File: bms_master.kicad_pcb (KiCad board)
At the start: 4 copper layers, 78 x 59 mm, 73 parts, among them J1 Conn_01x08, J2 I2C, J3 I2C, J4 CSENSE, J5 CSENSE, J6 SWD, SW1 SW_Push, U1 TPS7B88, U2 MCP1700x-330xxMB, U3 STM32F103C8Tx, U4 SN65HVD1050D, U5 M24C64-R, U6 MAX6126, U7 MAX11163, U8 741G3157, Y1 8M

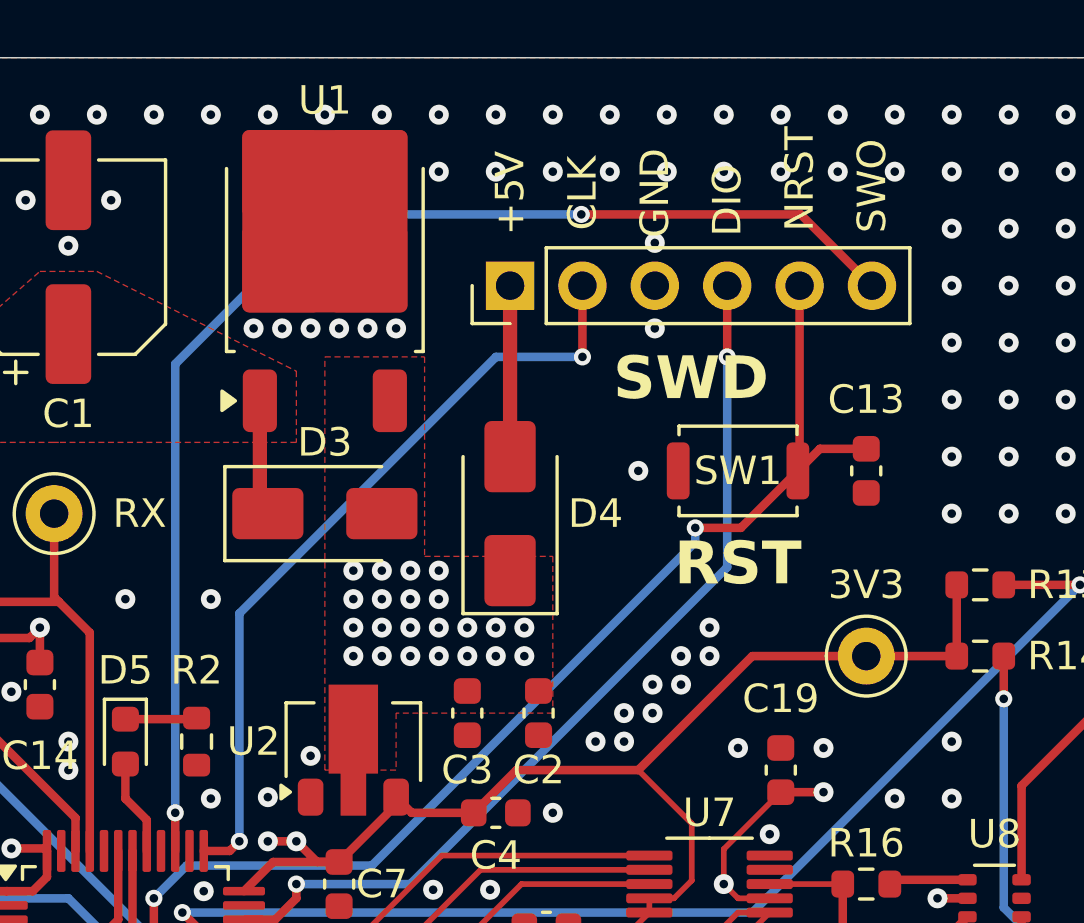
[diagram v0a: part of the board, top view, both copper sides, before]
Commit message: *: Update library references and move SWD header slightly
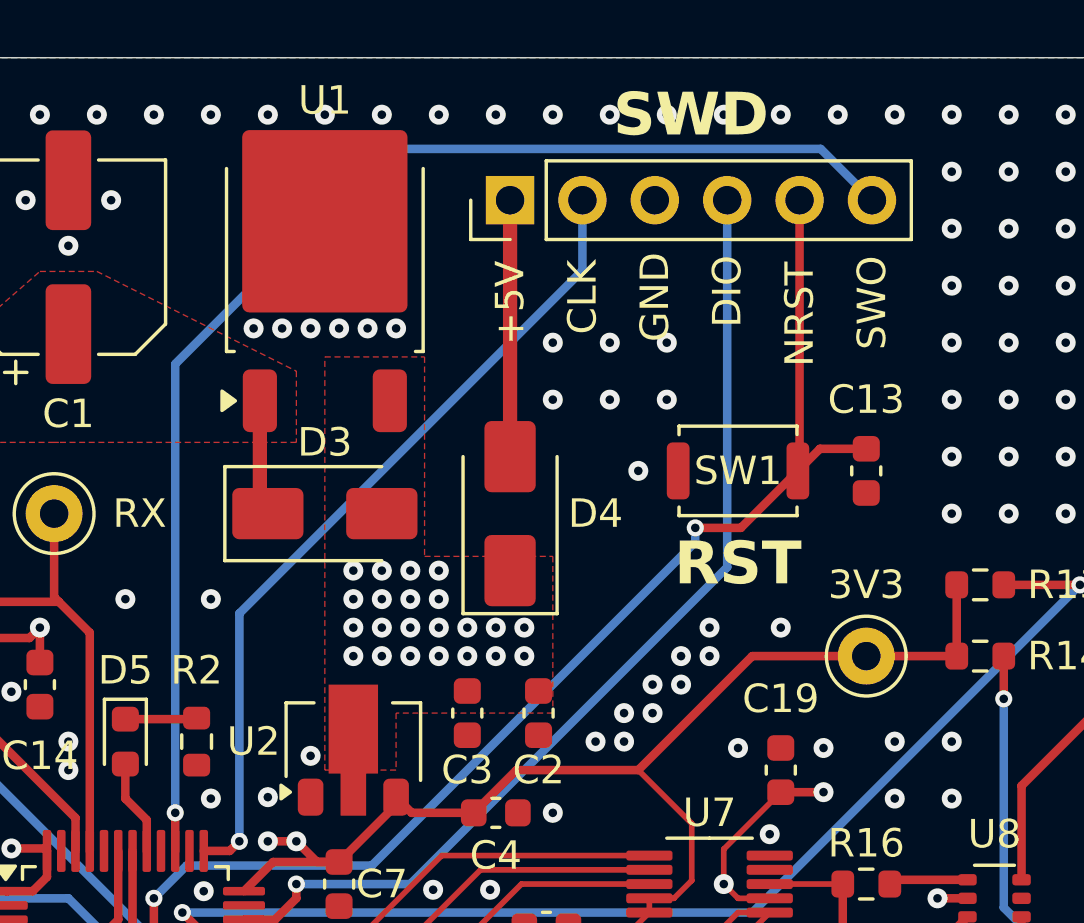
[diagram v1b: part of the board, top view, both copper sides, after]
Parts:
- moved J6 3.00 mm to (118.5, 35.0)
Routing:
- net Net-(D4-A): track 6.00 -> 9.00 mm
- net /SWDIO: track 32.3 -> 35.3 mm, vias 2 -> 1
- net /NRST: track 48.5 -> 51.5 mm
- net /SWCLK: track 27.7 -> 28.9 mm, vias 2 -> 1
- net /SWO: track 44.7 -> 45.4 mm, vias 2 -> 1
- net GND: vias 471 -> 468

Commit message: *: Change all 100k pull-up and pull-downs to 10k
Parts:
- R12, R13, R14, R15, R3, R4: value 100k -> 10k
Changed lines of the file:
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@@
 			)
 		)
-		(property "Value" "100k"
+		(property "Value" "10k"
 			(at 0 1.43 0)
 			(layer "F.Fab")
@@
 			)
 		)
-		(property "Dist #" "C25803"
+		(property "Dist #" "C25804"
 			(at 0 0 0)
 			(unlocked yes)
@@
 			)
 		)
-		(property "Mfr #" "0603WAF1003T5E"
+		(property "Mfr #" "0603WAF1002T5E"
 			(at 0 0 0)
 			(unlocked yes)
@@
 			)
 		)
-		(property "Value" "100k"
+		(property "Value" "10k"
 			(at 0 1.43 0)
 			(layer "F.Fab")
@@
 			)
 		)
-		(property "Dist #" "C25803"
+		(property "Dist #" "C25804"
 			(at 0 0 0)
 			(unlocked yes)
@@
 			)
 		)
-		(property "Mfr #" "0603WAF1003T5E"
+		(property "Mfr #" "0603WAF1002T5E"
 			(at 0 0 0)
 			(unlocked yes)
@@
 			)
 		)
-		(property "Value" "100k"
+		(property "Value" "10k"
 			(at 0 1.43 90)
 			(layer "F.Fab")
@@
 			)
 		)
-		(property "Dist #" "C25803"
+		(property "Dist #" "C25804"
 			(at 0 0 270)
 			(unlocked yes)
@@
 			)
 		)
-		(property "Mfr #" "0603WAF1003T5E"
+		(property "Mfr #" "0603WAF1002T5E"
 			(at 0 0 270)
 			(unlocked yes)
@@
 			)
 		)
-		(property "Value" "100k"
+		(property "Value" "10k"
 			(at 0 1.43 90)
 			(layer "F.Fab")
@@
 			)
 		)
-		(property "Dist #" "C25803"
+		(property "Dist #" "C25804"
 			(at 0 0 90)
 			(unlocked yes)
@@
 			)
 		)
-		(property "Mfr #" "0603WAF1003T5E"
+		(property "Mfr #" "0603WAF1002T5E"
 			(at 0 0 90)
 			(unlocked yes)
@@
 			)
 		)
-		(property "Value" "100k"
+		(property "Value" "10k"
 			(at 0 1.43 90)
 			(layer "F.Fab")
@@
 			)
 		)
-		(property "Dist #" "C25803"
+		(property "Dist #" "C25804"
 			(at 0 0 90)
 			(unlocked yes)
@@
 			)
 		)
-		(property "Mfr #" "0603WAF1003T5E"
+		(property "Mfr #" "0603WAF1002T5E"
 			(at 0 0 90)
 			(unlocked yes)
@@
 			)
 		)
-		(property "Value" "100k"
+		(property "Value" "10k"
 			(at 0 1.43 0)
 			(layer "F.Fab")
@@
 			)
 		)
-		(property "Dist #" "C25803"
+		(property "Dist #" "C25804"
 			(at 0 0 180)
 			(unlocked yes)
@@
 			)
 		)
-		(property "Mfr #" "0603WAF1003T5E"
+		(property "Mfr #" "0603WAF1002T5E"
 			(at 0 0 180)
 			(unlocked yes)

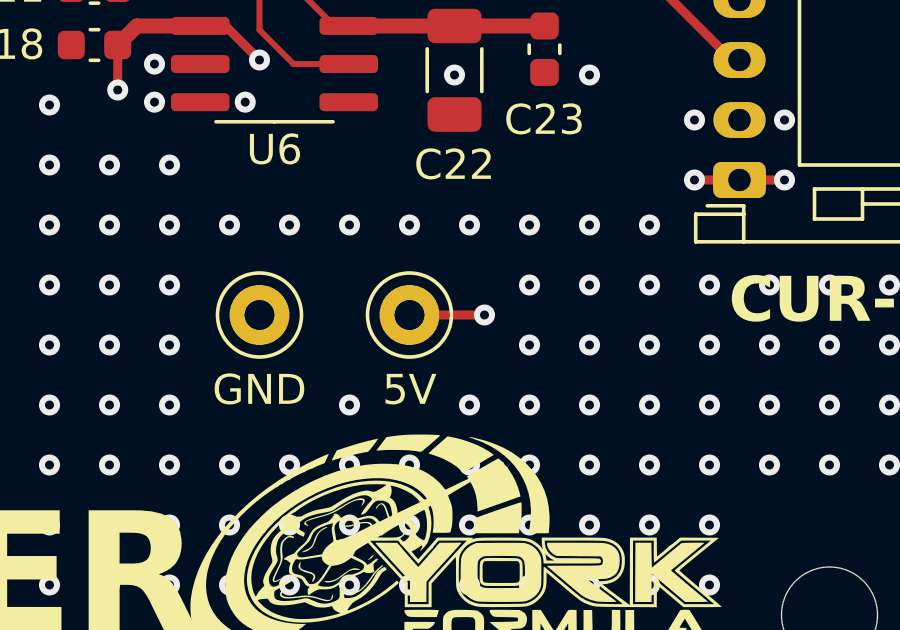
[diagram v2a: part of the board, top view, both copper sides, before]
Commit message: pcb: Remove unnecessary 5V via for test point
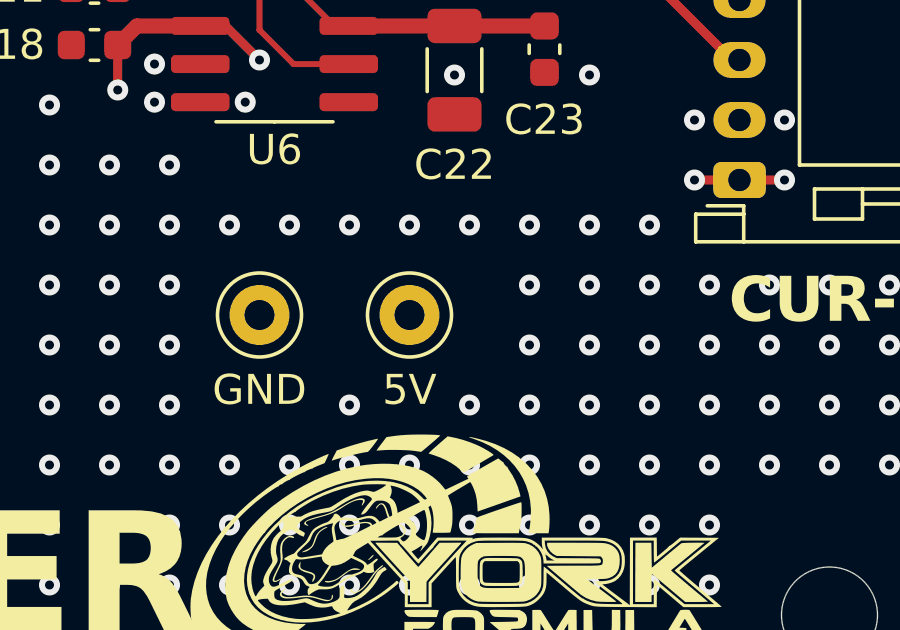
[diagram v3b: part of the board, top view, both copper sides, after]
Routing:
- net +5V: track 50.0 -> 47.5 mm, vias 45 -> 44
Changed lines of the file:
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@@
-	)
-	(segment
-		(start 132.5 75)
-		(end 130 75)
-		(width 0.3)
-		(layer "F.Cu")
-		(net 3)
 	)
 	(segment
@@
 		(size 0.7)
 		(drill 0.3)
-		(layers "F.Cu" "B.Cu")
-		(free yes)
-		(net 3)
-	)
-	(via
-		(at 132.5 75)
-		(size 0.7)
-		(drill 0.3)

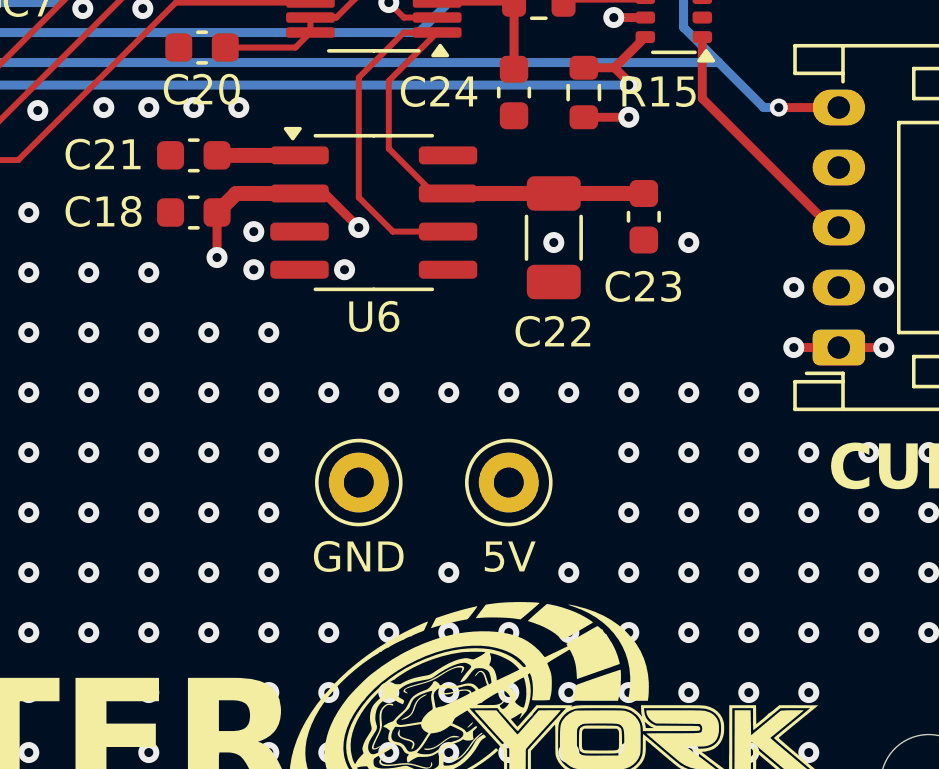
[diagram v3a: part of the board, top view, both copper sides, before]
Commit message: *: Add a test point for the reference
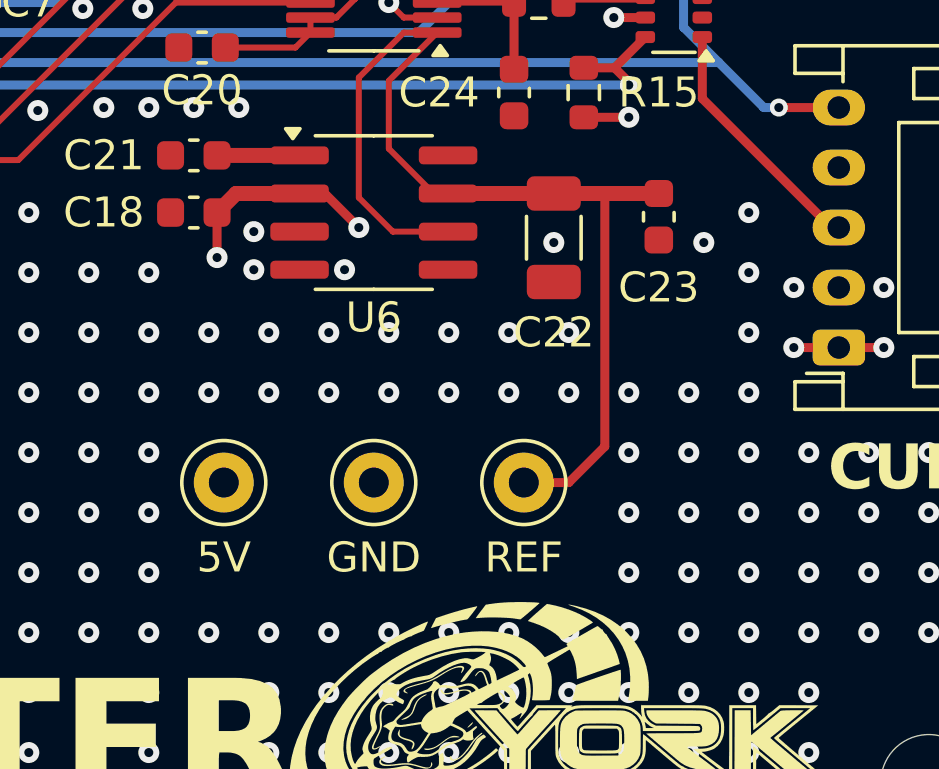
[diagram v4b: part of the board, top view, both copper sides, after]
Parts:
- added TP6: TestPoint, TestPoint:TestPoint_Keystone_5000-5004_Miniature, F.Cu at (130.5, 75.0)
- moved TP2 9.50 mm to (120.5, 75.0)
- moved C23 0.50 mm to (135.0, 66.1)
- moved TP1 0.50 mm to (125.5, 75.0)
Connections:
- net Net-(U6-OUTF) renamed /REF
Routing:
- net /REF: track 23.9 -> 36.0 mm
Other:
- board text added: "REF"

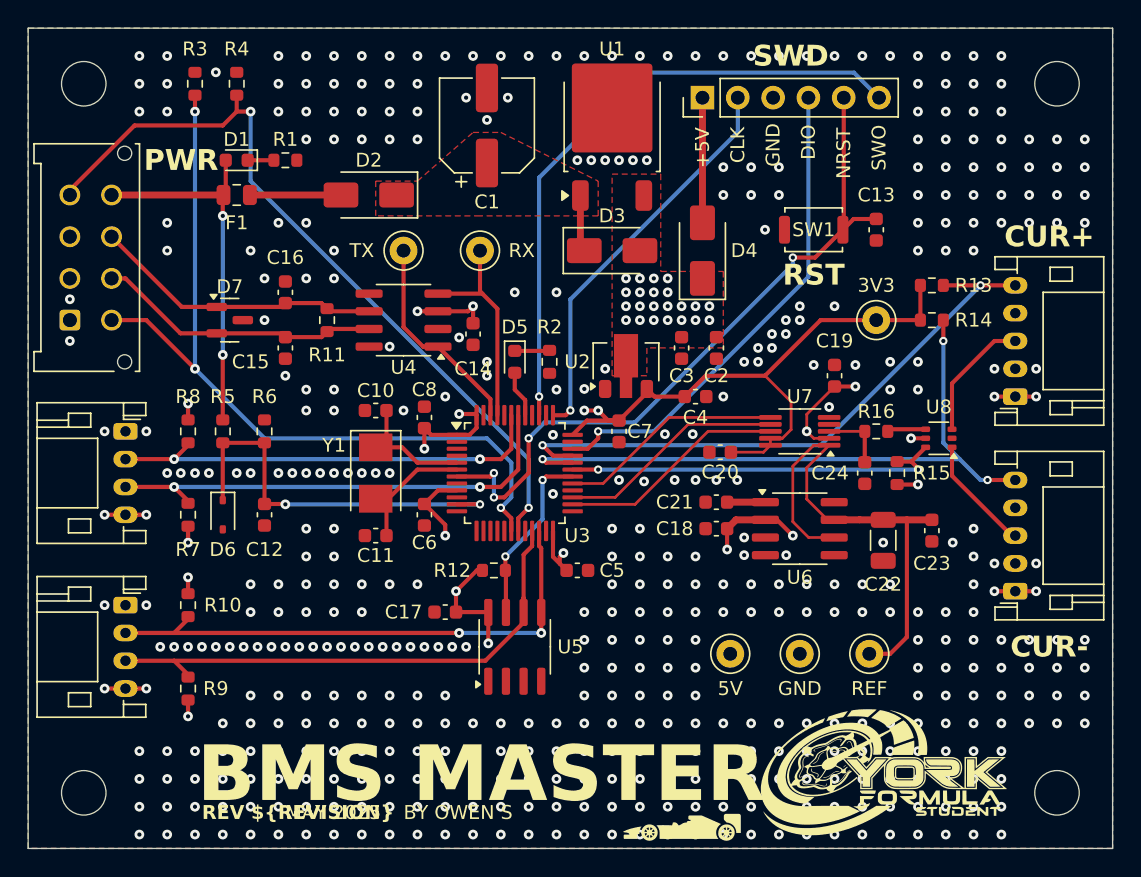
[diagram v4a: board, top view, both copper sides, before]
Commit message: *: Mirror I2C connector pin order
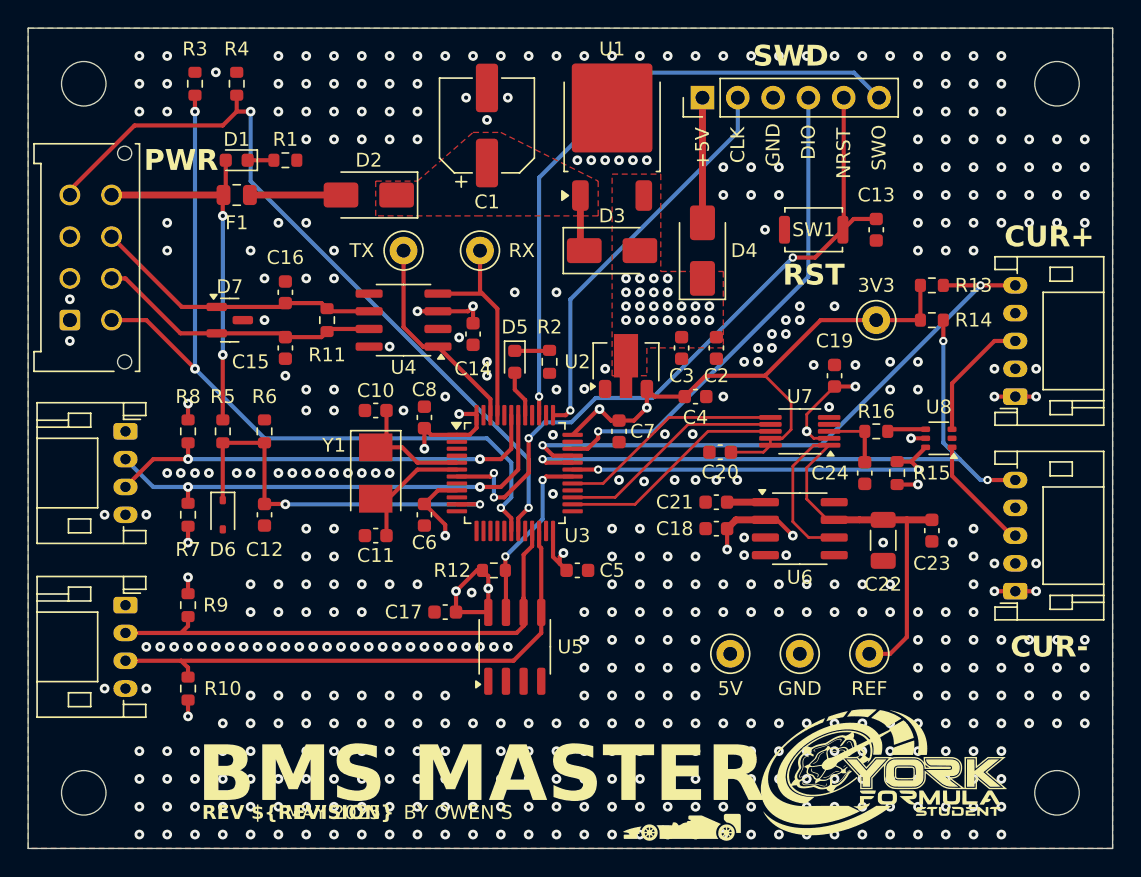
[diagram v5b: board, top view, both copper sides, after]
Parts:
- moved R10 6.00 mm to (81.5, 77.5), turned to 90 degrees
- moved R9 6.00 mm to (81.5, 71.5), turned to -90 degrees
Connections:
- J2 pad 1: GND -> +5V
- J2 pad 2: SDA1 -> SCL1
- J2 pad 3: SCL1 -> SDA1
- J2 pad 4: +5V -> GND
- J3 pad 1: GND -> +5V
- J3 pad 2: SDA2 -> SCL2
- J3 pad 3: SCL2 -> SDA2
- J3 pad 4: +5V -> GND
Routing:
- net +5V: track 47.5 -> 42.5 mm, vias 44 -> 40
- net +3V3: track 61.6 -> 60.4 mm
- net SDA2: track 38.7 -> 39.5 mm, vias 2 -> 0
- net SDA1: track 31.9 -> 32.5 mm
- net SCL1: track 34.1 -> 34.7 mm
- net GND: vias 468 -> 473
